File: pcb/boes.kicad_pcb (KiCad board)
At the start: 2 copper layers, 61 x 76.2 mm, 17 parts, among them J1 SW_A, J10 HUB75 Display ctrl, J2 SW_B, J3 SW_C, J4 Pot_J, J6 Sens_J, J7 Sens_P, J8 Buzzer, J9 Display power, Q1 2N7000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

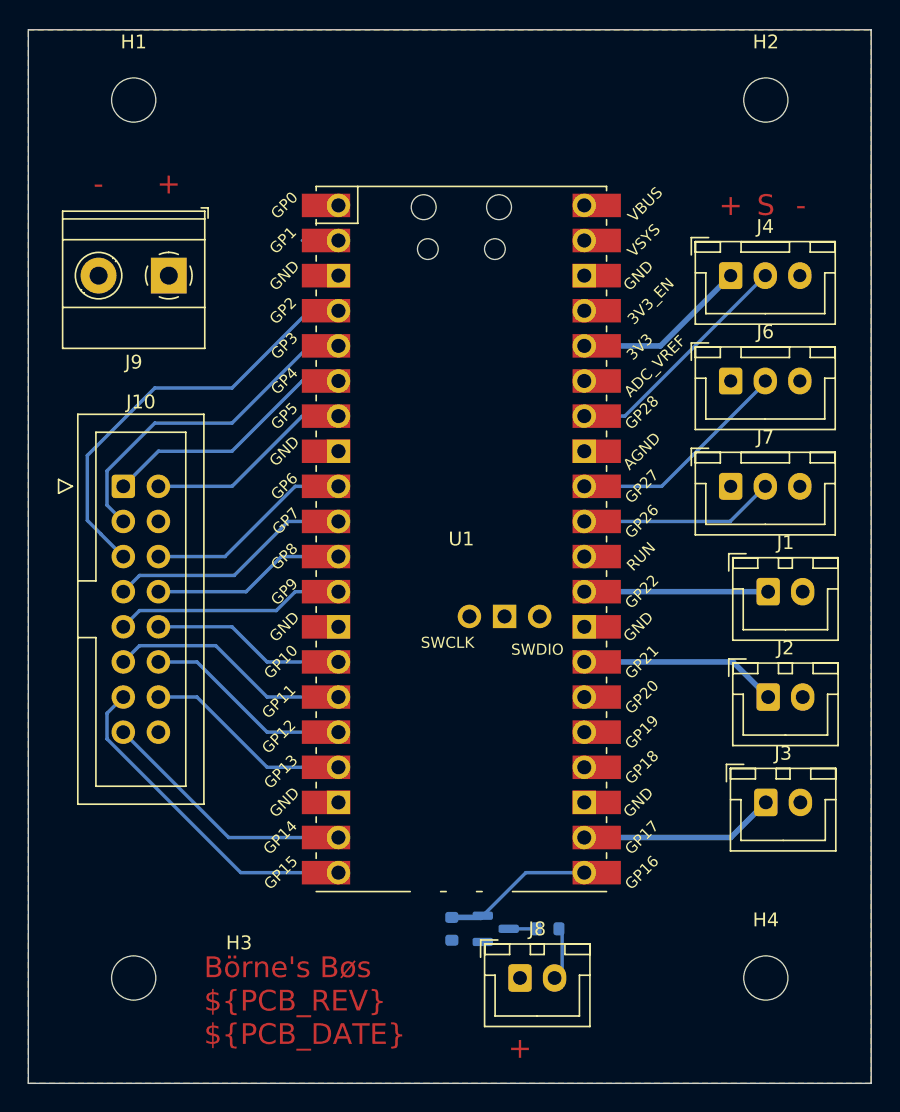
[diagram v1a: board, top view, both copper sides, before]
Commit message: Repurpose screw terminal as input
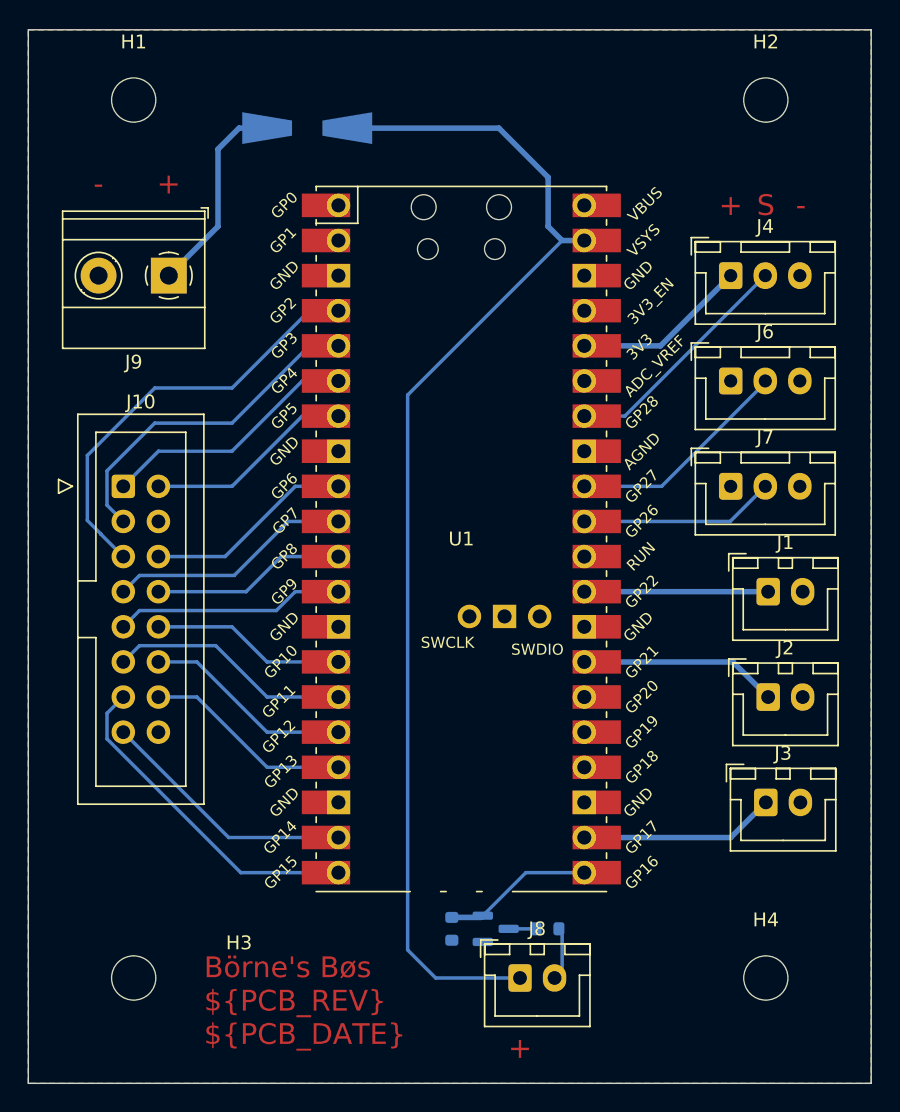
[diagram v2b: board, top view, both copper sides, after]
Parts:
- added D1: D_Schottky, Diode_SMD:D_SMA-SMB_Universal_Handsoldering, B.Cu at (114.2, 57.9)
- J9: value Display power -> +5V External
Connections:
- J8 pad 1: +5V -> VCC
- J9 pad 1: +5V -> Net-(D1-A)
- U1 pad 39: unconnected-(U1-Pad39) -> VCC
- U1 pad 40: +5V -> unconnected-(U1-VBUS-Pad40)
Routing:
- net VCC: track 0.00 -> 87.5 mm
- net Net-(D1-A): track 0.00 -> 13.3 mm
- net unconnected-(U1-GPIO1-Pad2): track 2.62 -> 0.00 mm

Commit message: Add teardrops to last change
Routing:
- net Net-(D1-A): track 13.3 -> 14.8 mm
